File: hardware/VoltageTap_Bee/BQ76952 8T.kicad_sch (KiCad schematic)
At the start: 113 parts, among them U201 2PD2150-QX, U202 2PD2150-QX, U203 2PD2150-QX, U204 2PD2150-QX, U205 2PD2150-QX, U206 2PD2150-QX, U207 2PD2150-QX, U208 2PD2150-QX, U209 2PD2150-QX, U210 2PD2150-QX, U211 2PD2150-QX, U212 2PD2150-QX, U213 2PD2150-QX, U214 2PD2150-QX, U215 2PD2150-QX, U216 2PD2150-QX, U217 PBQ76952PFBT, U218 FCX495

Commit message: This is a cry for help
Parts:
- removed D218: ES1D, Diode_SMD:D_SMA, symbol Device:D_Schottky_Small
- removed R255: 100, Resistor_SMD:R_0805_2012Metric, symbol Device:R_Small_US
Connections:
- net 16P: now also U218.2
- net BAT: now also C221.1
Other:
- note removed: "joined to prevent absurd voltage differences"
- moved on the sheet: C220, C221

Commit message: uhhh
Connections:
- net 16P: no longer R253.2, R254.1, U218.2
- net at D217.1 (K), R252.2: now also R253.2, R254.1, U218.2
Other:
- added sheet something (../common designs.kicad_sch)
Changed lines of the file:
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@@
 	)
 	(junction
-		(at 246.38 16.51)
-		(diameter 0)
-		(color 0 0 0 0)
-	)
-	(junction
 		(at 127 114.3)
 		(diameter 0)
@@
 	)
 	(junction
+		(at 246.38 26.67)
+		(diameter 0)
+		(color 0 0 0 0)
+	)
+	(junction
 		(at 149.86 96.52)
 		(diameter 0)
@@
 	(wire
 		(pts
-			(xy 262.89 16.51) (xy 262.89 72.39)
-		)
-		(stroke
-			(width 0)
-			(type default)
-		)
-	)
-	(wire
-		(pts
 			(xy 148.59 35.56) (xy 149.86 36.83)
 		)
@@
 	(wire
 		(pts
+			(xy 262.89 26.67) (xy 262.89 72.39)
+		)
+		(stroke
+			(width 0)
+			(type default)
+		)
+	)
+	(wire
+		(pts
 			(xy 196.85 59.69) (xy 198.12 59.69)
 		)
@@
 	(wire
 		(pts
-			(xy 246.38 16.51) (xy 262.89 16.51)
-		)
-		(stroke
-			(width 0)
-			(type default)
-		)
-	)
-	(wire
-		(pts
 			(xy 55.88 31.75) (xy 64.77 31.75)
 		)
@@
 	(wire
 		(pts
+			(xy 246.38 26.67) (xy 246.38 33.02)
+		)
+		(stroke
+			(width 0)
+			(type default)
+		)
+	)
+	(wire
+		(pts
 			(xy 55.88 130.81) (xy 55.88 132.08)
 		)
@@
 	(wire
 		(pts
+			(xy 246.38 26.67) (xy 262.89 26.67)
+		)
+		(stroke
+			(width 0)
+			(type default)
+		)
+	)
+	(wire
+		(pts
 			(xy 226.06 48.26) (xy 237.49 48.26)
 		)
@@
 	(wire
 		(pts
-			(xy 246.38 24.13) (xy 246.38 33.02)
+			(xy 246.38 24.13) (xy 246.38 26.67)
 		)
 		(stroke
@@
 				)
 			)
+		)
+	)
+	(sheet
+		(at 347.98 172.72)
+		(size 27.94 22.86)
+		(exclude_from_sim yes)
+		(in_bom no)
+		(on_board no)
+		(dnp yes)
+		(fields_autoplaced yes)
+		(stroke
+			(width 0.1524)
+			(type solid)
+		)
+		(fill
+			(color 0 0 0 0.0000)
+		)
+		(property "Sheetname" "something"
+			(at 347.98 172.0084 0)
+			(effects
+				(font
+					(size 1.27 1.27)
+				)
+				(justify left bottom)
+			)
+		)
+		(property "Sheetfile" "../common designs.kicad_sch"
+			(at 347.98 196.1646 0)
+			(effects
+				(font
+					(size 1.27 1.27)
+				)
+				(justify left top)
+			)
+		)
+		(property "Field2" ""
+			(at 347.98 172.72 0)
+			(effects
+				(font
+					(size 1.27 1.27)
+				)
+			)
+		)
+		(instances
+			(project "VoltageTap_B"
+				(path "/24c6cb45-cbeb-4148-a23c-ec2e76234670/5ed1aefd-4d0e-4d3d-a5a2-f479b00e73a5"
+					(page "5")
+				)
+			)

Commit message: aenllaec
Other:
- removed sheet something
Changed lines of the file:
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@@
-		)
-	)
-	(sheet
-		(at 347.98 172.72)
-		(size 27.94 22.86)
-		(exclude_from_sim yes)
-		(in_bom no)
-		(on_board no)
-		(dnp yes)
-		(fields_autoplaced yes)
-		(stroke
-			(width 0.1524)
-			(type solid)
-		)
-		(fill
-			(color 0 0 0 0.0000)
-		)
-		(property "Sheetname" "something"
-			(at 347.98 172.0084 0)
-			(effects
-				(font
-					(size 1.27 1.27)
-				)
-				(justify left bottom)
-			)
-		)
-		(property "Sheetfile" "../common designs.kicad_sch"
-			(at 347.98 196.1646 0)
-			(effects
-				(font
-					(size 1.27 1.27)
-				)
-				(justify left top)
-			)
-		)
-		(property "Field2" ""
-			(at 347.98 172.72 0)
-			(effects
-				(font
-					(size 1.27 1.27)
-				)
-			)
-		)
-		(instances
-			(project "VoltageTap_B"
-				(path "/24c6cb45-cbeb-4148-a23c-ec2e76234670/5ed1aefd-4d0e-4d3d-a5a2-f479b00e73a5"
-					(page "999")
-				)
-			)
 		)
 	)

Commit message: baeckbjlnacnklac
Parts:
- renumbered R256 to R255
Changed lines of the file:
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@@
 		(on_board yes)
 		(dnp no)
-		(property "Reference" "R256"
+		(property "Reference" "R255"
 			(at 274.828 82.55 0)
 			(effects
@@
 			(project "VoltageTap_B"
 				(path "/24c6cb45-cbeb-4148-a23c-ec2e76234670/5ed1aefd-4d0e-4d3d-a5a2-f479b00e73a5"
-					(reference "R256")
+					(reference "R255")
 					(unit 1)
 				)

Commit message: Fixing
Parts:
- R221, R222, R223, R224, R225, R226, R227, R245, R246, R247, R248, R249, R250, R251: mouser https://www.mouser.com/ProductDetail/KOA-Speer/RK73H2BTTD22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 -> https://www.mouser.com/ProductDetail/KOA-Speer/RK73H2ATTD22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
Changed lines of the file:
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@@
 			)
 		)
-		(property "mouser" "https://www.mouser.com/ProductDetail/KOA-Speer/RK73H2BTTD2260F?qs=sGAEpiMZZMvdGkrng054t0wRT%252B902PGcT6B0yBPcmBs%3D"
+		(property "mouser" "https://www.mouser.com/ProductDetail/KOA-Speer/RK73H2ATTD2260F?qs=MzOn2VpwozEuMvy0cV9RWw%3D%3D"
 			(at 67.31 147.32 0)
 			(effects
@@
 			)
 		)
-		(property "mouser" "https://www.mouser.com/ProductDetail/KOA-Speer/RK73H2BTTD2260F?qs=sGAEpiMZZMvdGkrng054t0wRT%252B902PGcT6B0yBPcmBs%3D"
+		(property "mouser" "https://www.mouser.com/ProductDetail/KOA-Speer/RK73H2ATTD2260F?qs=MzOn2VpwozEuMvy0cV9RWw%3D%3D"
 			(at 138.43 46.99 0)
 			(effects
@@
 			)
 		)
-		(property "mouser" "https://www.mouser.com/ProductDetail/KOA-Speer/RK73H2BTTD2260F?qs=sGAEpiMZZMvdGkrng054t0wRT%252B902PGcT6B0yBPcmBs%3D"
+		(property "mouser" "https://www.mouser.com/ProductDetail/KOA-Speer/RK73H2ATTD2260F?qs=MzOn2VpwozEuMvy0cV9RWw%3D%3D"
 			(at 138.43 96.52 0)
 			(effects
@@
 			)
 		)
-		(property "mouser" "https://www.mouser.com/ProductDetail/KOA-Speer/RK73H2BTTD2260F?qs=sGAEpiMZZMvdGkrng054t0wRT%252B902PGcT6B0yBPcmBs%3D"
+		(property "mouser" "https://www.mouser.com/ProductDetail/KOA-Speer/RK73H2ATTD2260F?qs=MzOn2VpwozEuMvy0cV9RWw%3D%3D"
 			(at 67.31 97.79 0)
 			(effects
@@
 			)
 		)
-		(property "mouser" "https://www.mouser.com/ProductDetail/KOA-Speer/RK73H2BTTD2260F?qs=sGAEpiMZZMvdGkrng054t0wRT%252B902PGcT6B0yBPcmBs%3D"
+		(property "mouser" "https://www.mouser.com/ProductDetail/KOA-Speer/RK73H2ATTD2260F?qs=MzOn2VpwozEuMvy0cV9RWw%3D%3D"
 			(at 67.31 163.83 0)
 			(effects
@@
 			)
 		)
-		(property "mouser" "https://www.mouser.com/ProductDetail/KOA-Speer/RK73H2BTTD2260F?qs=sGAEpiMZZMvdGkrng054t0wRT%252B902PGcT6B0yBPcmBs%3D"
+		(property "mouser" "https://www.mouser.com/ProductDetail/KOA-Speer/RK73H2ATTD2260F?qs=MzOn2VpwozEuMvy0cV9RWw%3D%3D"
 			(at 138.43 114.3 0)
 			(effects
@@
 			)
 		)
-		(property "mouser" "https://www.mouser.com/ProductDetail/KOA-Speer/RK73H2BTTD2260F?qs=sGAEpiMZZMvdGkrng054t0wRT%252B902PGcT6B0yBPcmBs%3D"
+		(property "mouser" "https://www.mouser.com/ProductDetail/KOA-Speer/RK73H2ATTD2260F?qs=MzOn2VpwozEuMvy0cV9RWw%3D%3D"
 			(at 138.43 130.81 0)
 			(effects
@@
 			)
 		)
-		(property "mouser" "https://www.mouser.com/ProductDetail/KOA-Speer/RK73H2BTTD2260F?qs=sGAEpiMZZMvdGkrng054t0wRT%252B902PGcT6B0yBPcmBs%3D"
+		(property "mouser" "https://www.mouser.com/ProductDetail/KOA-Speer/RK73H2ATTD2260F?qs=MzOn2VpwozEuMvy0cV9RWw%3D%3D"
 			(at 138.43 63.5 0)
 			(effects
@@
 			)
 		)
-		(property "mouser" "https://www.mouser.com/ProductDetail/KOA-Speer/RK73H2BTTD2260F?qs=sGAEpiMZZMvdGkrng054t0wRT%252B902PGcT6B0yBPcmBs%3D"
+		(property "mouser" "https://www.mouser.com/ProductDetail/KOA-Speer/RK73H2ATTD2260F?qs=MzOn2VpwozEuMvy0cV9RWw%3D%3D"
 			(at 138.43 80.01 0)
 			(effects
@@
 			)
 		)
-		(property "mouser" "https://www.mouser.com/ProductDetail/KOA-Speer/RK73H2BTTD2260F?qs=sGAEpiMZZMvdGkrng054t0wRT%252B902PGcT6B0yBPcmBs%3D"
+		(property "mouser" "https://www.mouser.com/ProductDetail/KOA-Speer/RK73H2ATTD2260F?qs=MzOn2VpwozEuMvy0cV9RWw%3D%3D"
 			(at 67.31 130.81 0)
 			(effects
@@
 			)
 		)
-		(property "mouser" "https://www.mouser.com/ProductDetail/KOA-Speer/RK73H2BTTD2260F?qs=sGAEpiMZZMvdGkrng054t0wRT%252B902PGcT6B0yBPcmBs%3D"
+		(property "mouser" "https://www.mouser.com/ProductDetail/KOA-Speer/RK73H2ATTD2260F?qs=MzOn2VpwozEuMvy0cV9RWw%3D%3D"
 			(at 67.31 64.77 0)
 			(effects
@@
 			)
 		)
-		(property "mouser" "https://www.mouser.com/ProductDetail/KOA-Speer/RK73H2BTTD2260F?qs=sGAEpiMZZMvdGkrng054t0wRT%252B902PGcT6B0yBPcmBs%3D"
+		(property "mouser" "https://www.mouser.com/ProductDetail/KOA-Speer/RK73H2ATTD2260F?qs=MzOn2VpwozEuMvy0cV9RWw%3D%3D"
 			(at 67.31 114.3 0)
 			(effects
@@
 			)
 		)
-		(property "mouser" "https://www.mouser.com/ProductDetail/KOA-Speer/RK73H2BTTD2260F?qs=sGAEpiMZZMvdGkrng054t0wRT%252B902PGcT6B0yBPcmBs%3D"
+		(property "mouser" "https://www.mouser.com/ProductDetail/KOA-Speer/RK73H2ATTD2260F?qs=MzOn2VpwozEuMvy0cV9RWw%3D%3D"
 			(at 67.31 81.28 0)
 			(effects
@@
 			)
 		)
-		(property "mouser" "https://www.mouser.com/ProductDetail/KOA-Speer/RK73H2BTTD2260F?qs=sGAEpiMZZMvdGkrng054t0wRT%252B902PGcT6B0yBPcmBs%3D"
+		(property "mouser" "https://www.mouser.com/ProductDetail/KOA-Speer/RK73H2ATTD2260F?qs=MzOn2VpwozEuMvy0cV9RWw%3D%3D"
 			(at 138.43 147.32 0)
 			(effects

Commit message: added part numbers for mouser
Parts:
- C203, C204, C205, C206, C207, C208, C209, C211, C212, C213, C214, C215, C216, C217: Mouser Part Number (none) -> 710-885012206095
- C219: Mouser Part Number (none) -> 187-CL31A106KBHNNNE
- C220, C221: Mouser Part Number (none) -> 187-CL31B105KCHNNNE
- D203, D204, D205, D206, D207, D208, D209, D210, D211, D212, D213, D214, D215, D216: Mouser Part Number (none) -> 821-TS4148RBG
- D217: Mouser Part Number (none) -> 512-ES1C
- R203, R204, R205, R206, R207, R208, R209, R228, R229, R230, R231, R232, R233, R234: Mouser Part Number (none) -> 755-LTR100JZPJ360
- R212, R213, R214, R215, R216, R217, R218, R237, R238, R239, R240, R241, R242, R243, R244, R252: Mouser Part Number (none) -> 660-SG73S2ATTD101J
- R221, R222, R223, R224, R225, R226, R227, R245, R246, R247, R248, R249, R250, R251: Mouser Part Number (none) -> 660-RK73H2ATTD2260F
- R253, R255: Mouser Part Number (none) -> 603-AC0805FR-7W10KL
- R254: Mouser Part Number (none) -> 708-RNCP1206FTD4K99
- U203, U204, U205, U206, U207, U208, U209, U210, U211, U212, U213, U214, U215, U216: Mouser Part Number (none) -> 771-2PD2150-QX
- U217: Mouser Part Number (none) -> 595-BQ7697204PFBR
- U218: Mouser Part Number (none) -> 522-FCX495TA

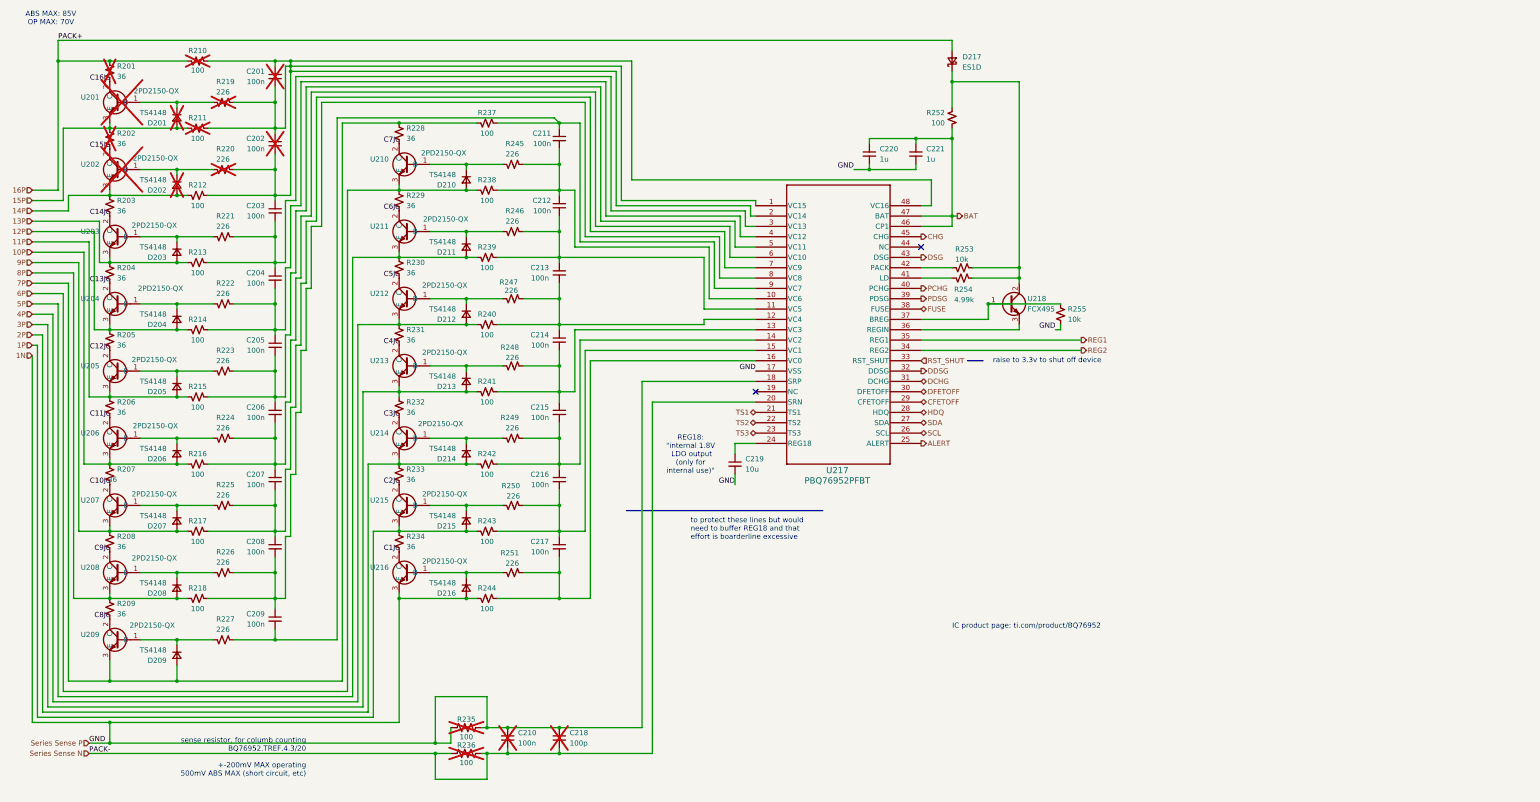
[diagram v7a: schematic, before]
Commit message: rework vt bee
UTA, where CpEs cant make a pcb and CSs cant write any code.
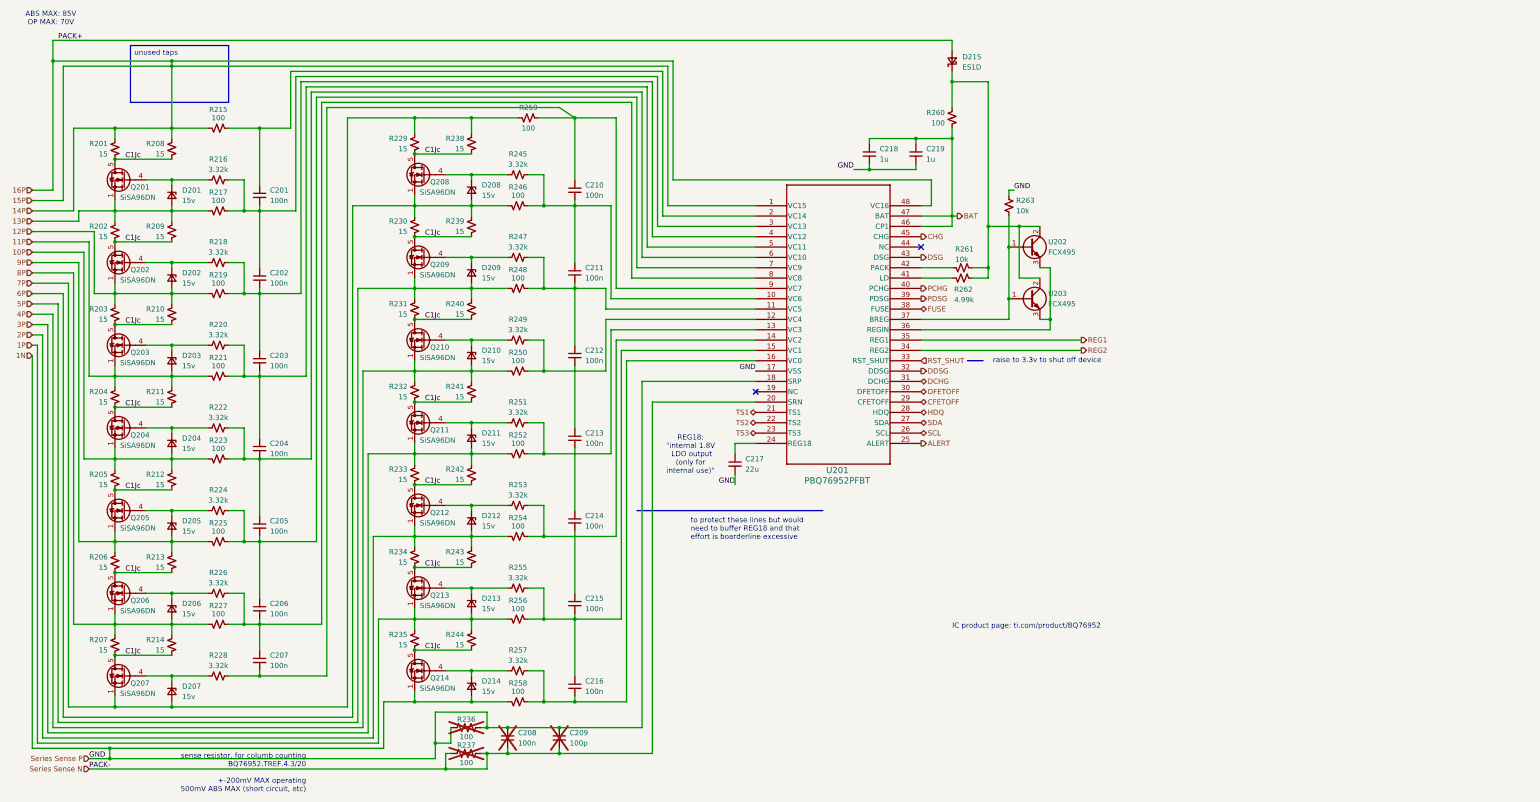
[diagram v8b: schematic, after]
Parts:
- removed C201, C202, C205, C216: 100n, Capacitor_SMD:C_0603_1608Metric_Pad1.08x0.95mm_HandSolder, symbol Device:C_Small
- removed C219: 10u, Capacitor_SMD:C_1206_3216Metric_Pad1.33x1.80mm_HandSolder, symbol Device:C_Small
- removed D201, D202, D203, D204, D205, D206, D207, D208, D209, D210, D211, D212, D213, D214, D215, D216: TS4148, Diode_SMD:D_0805_2012Metric_Pad1.15x1.40mm_HandSolder, symbol Device:D_Small
- removed U201, U202, U203, U204, U205, U206, U207, U208, U209, U210, U211, U212, U213, U214, U215, U216: 2PD2150-QX, Package_TO_SOT_SMD:SOT-89-3, symbol zzLocalLibrary:2PD2150-QX
- added C207, C210: 100n, Capacitor_SMD:C_0603_1608Metric_Pad1.08x0.95mm_HandSolder, symbol Device:C_Small
- added C217: 22u, Capacitor_SMD:C_0805_2012Metric_Pad1.18x1.45mm_HandSolder, symbol Device:C_Small
- added D201, D202, D203, D204, D205, D206, D207, D208, D209, D210, D211, D212, D213, D214: 15v, Diode_SMD:D_SOD-123, symbol Device:D_Zener_Small
- added Q201, Q202, Q203, Q204, Q205, Q206, Q207, Q208, Q209, Q210, Q211, Q212, Q213, Q214: SiSA96DN, Package_SO:Vishay_PowerPAK_1212-8_Single, symbol Transistor_FET:SiS454DN
- added R234, R244: 15, zzLocalLibraries-Footprints:imperial wide resistor R_ 3264, symbol Device:R_Small_US
- added R252, R254, R256: 100, Resistor_SMD:R_0805_2012Metric, symbol Device:R_Small_US
- added R253, R255, R257: 3.32k, Resistor_SMD:R_0805_2012Metric_Pad1.20x1.40mm_HandSolder, symbol Device:R_Small_US
- added U203: FCX495, Package_TO_SOT_SMD:SOT-89-3, symbol zzLocalLibrary:FCX485_NPN_BJT
- R201, R202: value 36 -> 15; Mouser Part Number (none) -> 755-LTR100JZPJ360; mouser https://www.mouser.com/ProductDetail/ROHM-Semiconductor/LTR100JZPJ360?qs=sGAEpiMZZMvdGkrng054tx4c7YuULGmGPstrAxlE1rsJ3%252BFyNXvM0g%3D%3D -> https://www.mouser.com/ProductDetail/ROHM-Semiconductor/LTR100JZPJ150?qs=Y0Uzf4wQF3lnWrANyJBr0A%3D%3D; specs 36 ohm, 3W, 200V, 1%, surge, wide. 200ppm, -55C, +155C -> 15 ohm, 3W, 200V, 1%, surge, wide. 200ppm, -55C, +155C; now fitted; now in the parts list
- R203, R204, R205, R206, R207, R208, R209, R229, R230, R231, R232, R233: value 36 -> 15; mouser https://www.mouser.com/ProductDetail/ROHM-Semiconductor/LTR100JZPJ360?qs=sGAEpiMZZMvdGkrng054tx4c7YuULGmGPstrAxlE1rsJ3%252BFyNXvM0g%3D%3D -> https://www.mouser.com/ProductDetail/ROHM-Semiconductor/LTR100JZPJ150?qs=Y0Uzf4wQF3lnWrANyJBr0A%3D%3D; specs 36 ohm, 3W, 200V, 1%, surge, wide. 200ppm, -55C, +155C -> 15 ohm, 3W, 200V, 1%, surge, wide. 200ppm, -55C, +155C
- R210, R211: value 100 -> 15; footprint Resistor_SMD:R_0805_2012Metric -> zzLocalLibraries-Footprints:imperial wide resistor R_ 3264; Mouser Part Number (none) -> 755-LTR100JZPJ360; mouser https://www.mouser.com/ProductDetail/KOA-Speer/SG73S2ATTD10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 -> https://www.mouser.com/ProductDetail/ROHM-Semiconductor/LTR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; specs 100 omh, thick, anti surge, 5%, 750mW, 400V, -55C, +155C, 1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 -> 15 ohm, 3W, 200V, 1%, surge, wide. 200ppm, -55C, +155C; unit x1 0.12 -> 0.60; unit x10 0.037 -> 0.265; unit x100 (none) -> 0.214; now fitted; now in the parts list
- R212, R213, R214, R238, R239, R240, R241, R242, R243: value 100 -> 15; footprint Resistor_SMD:R_0805_2012Metric -> zzLocalLibraries-Footprints:imperial wide resistor R_ 3264; Mouser Part Number 660-SG73S2ATTD101J -> 755-LTR100JZPJ360; mouser https://www.mouser.com/ProductDetail/KOA-Speer/SG73S2ATTD10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 -> https://www.mouser.com/ProductDetail/ROHM-Semiconductor/LTR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; specs 100 omh, thick, anti surge, 5%, 750mW, 400V, -55C, +155C, 1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 -> 15 ohm, 3W, 200V, 1%, surge, wide. 200ppm, -55C, +155C; unit x1 0.12 -> 0.60; unit x10 0.037 -> 0.265; unit x100 (none) -> 0.214
- R216, R218: value 100 -> 3.32k; footprint Resistor_SMD:R_0805_2012Metric -> Resistor_SMD:R_0805_2012Metric_Pad1.20x1.40mm_HandSolder; Mouser Part Number 660-SG73S2ATTD101J -> (none); mouser https://www.mouser.com/ProductDetail/KOA-Speer/SG73S2ATTD10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 -> https://www.mouser.com/ProductDetail/Walsin/WR08X3321FTL?qs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; specs 100 omh, thick, anti surge, 5%, 750mW, 400V, -55C, +155C, 1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 -> 3.32kOhm, 1%, 150V, 125mW, 100ppm, -55C, 155C; unit x1 0.12 -> 0.10; unit x10 0.037 -> .025
- R219: value 226 -> 100; footprint Resistor_SMD:R_0805_2012Metric_Pad1.20x1.40mm_HandSolder -> Resistor_SMD:R_0805_2012Metric; Mouser Part Number (none) -> 660-SG73S2ATTD101J; mouser https://www.mouser.com/ProductDetail/KOA-Speer/RK73H2BTTD22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 -> https://www.mouser.com/ProductDetail/KOA-Speer/SG73S2ATTD10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; specs 226Ohm, 250mW, 1%, 200V, -55C, +155C -> 100 omh, thick, anti surge, 5%, 750mW, 400V, -55C, +155C, 1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; unit x1 0.10 -> 0.12; unit x10 0.023 -> 0.037; now fitted; now in the parts list
- R220: value 226 -> 3.32k; mouser https://www.mouser.com/ProductDetail/KOA-Speer/RK73H2BTTD22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 -> https://www.mouser.com/ProductDetail/Walsin/WR08X3321FTL?qs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; specs 226Ohm, 250mW, 1%, 200V, -55C, +155C -> 3.32kOhm, 1%, 150V, 125mW, 100ppm, -55C, 155C; unit x10 0.023 -> .025; now fitted; now in the parts list
- R221, R223, R225, R227, R246, R248, R250: value 226 -> 100; footprint Resistor_SMD:R_0805_2012Metric_Pad1.20x1.40mm_HandSolder -> Resistor_SMD:R_0805_2012Metric; Mouser Part Number 660-RK73H2ATTD2260F -> 660-SG73S2ATTD101J; mouser https://www.mouser.com/ProductDetail/KOA-Speer/RK73H2ATTD22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 -> https://www.mouser.com/ProductDetail/KOA-Speer/SG73S2ATTD10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; specs 226Ohm, 250mW, 1%, 200V, -55C, +155C -> 100 omh, thick, anti surge, 5%, 750mW, 400V, -55C, +155C, 1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; unit x1 0.10 -> 0.12; unit x10 0.023 -> 0.037
- R222, R224, R226, R245, R247, R249, R251: value 226 -> 3.32k; Mouser Part Number 660-RK73H2ATTD2260F -> (none); mouser https://www.mouser.com/ProductDetail/KOA-Speer/RK73H2ATTD22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 -> https://www.mouser.com/ProductDetail/Walsin/WR08X3321FTL?qs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; specs 226Ohm, 250mW, 1%, 200V, -55C, +155C -> 3.32kOhm, 1%, 150V, 125mW, 100ppm, -55C, 155C; unit x10 0.023 -> .025
- R228: value 36 -> 3.32k; footprint zzLocalLibraries-Footprints:imperial wide resistor R_ 3264 -> Resistor_SMD:R_0805_2012Metric_Pad1.20x1.40mm_HandSolder; Mouser Part Number 755-LTR100JZPJ360 -> (none); mouser https://www.mouser.com/ProductDetail/ROHM-Semiconductor/LTR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 -> https://www.mouser.com/ProductDetail/Walsin/WR08X3321FTL?qs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; specs 36 ohm, 3W, 200V, 1%, surge, wide. 200ppm, -55C, +155C -> 3.32kOhm, 1%, 150V, 125mW, 100ppm, -55C, 155C; unit x1 0.60 -> 0.10; unit x10 0.265 -> .025; unit x100 0.214 -> (none)
- R235: renamed from R234; value 36 -> 15; mouser https://www.mouser.com/ProductDetail/ROHM-Semiconductor/LTR100JZPJ360?qs=sGAEpiMZZMvdGkrng054tx4c7YuULGmGPstrAxlE1rsJ3%252BFyNXvM0g%3D%3D -> https://www.mouser.com/ProductDetail/ROHM-Semiconductor/LTR100JZPJ150?qs=Y0Uzf4wQF3lnWrANyJBr0A%3D%3D; specs 36 ohm, 3W, 200V, 1%, surge, wide. 200ppm, -55C, +155C -> 15 ohm, 3W, 200V, 1%, surge, wide. 200ppm, -55C, +155C
- renumbered C203 to C201, C204 to C202, C206 to C203, C207 to C204, C208 to C205, C209 to C206, C210 to C208, C218 to C209, C217 to C216, C220 to C218, C221 to C219, D217 to D215, R235 to R236, R236 to R237, R244 to R258, R237 to R259, R252 to R260, R253 to R261, R254 to R262, R255 to R263, U217 to U201, U218 to U202
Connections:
- net C10Jc is gone; now on net C1Jc: R207.1
- net C11Jc is gone; now on net C1Jc: R206.1
- net C12Jc is gone; now on net C1Jc: R205.1
- net C13Jc is gone; now on net C1Jc: R204.1
- net C14Jc is gone; now on net C1Jc: R203.1
- net C15Jc is gone; now on net C1Jc: R202.1
- net C16Jc is gone; now on net C1Jc: R201.1
- net C2Jc is gone; now on net C1Jc: R233.1
- net C3Jc is gone; now on net C1Jc: R232.1
- net C4Jc is gone; now on net C1Jc: R231.1
- net C5Jc is gone; now on net C1Jc: R230.1
- net C6Jc is gone; now on net C1Jc: R229.1
- net C8Jc is gone; now on net C1Jc: R209.1
- net C9Jc is gone; now on net C1Jc: R208.1
- net 10P: now also R205.2, R212.2, R223.2, D204.2 (A), Q204.1 (S), Q204.2 (S), Q204.3 (S); no longer R207.2, R216.2
- net 11P: now also R204.2, R211.2, R221.2, D203.2 (A), Q203.1 (S), Q203.2 (S), Q203.3 (S); no longer R206.2, R215.2
- net 12P: now also R203.2, R210.2, R219.2, D202.2 (A), Q202.1 (S), Q202.2 (S), Q202.3 (S); no longer R205.2, R214.2
- net 13P: now also R202.2, R209.2, R217.2, D201.2 (A), Q201.1 (S), Q201.2 (S), Q201.3 (S); no longer R204.2, R213.2
- net 14P: now also D215.2 (A), R201.2, R208.2, R215.2, U201.1 (VC15), U201.48 (VC16); no longer R203.2, R212.2
- net 1N: now also R263.2, C217.2, D214.2 (A), Q214.1 (S), Q214.2 (S), Q214.3 (S); no longer R263.1
- net 1P: now also D213.2 (A), Q213.1 (S), Q213.2 (S), Q213.3 (S), R244.2, R256.2; no longer R243.2
- net 2P: now also R243.2, D212.2 (A), Q212.1 (S), Q212.2 (S), Q212.3 (S), R234.2, R254.2; no longer R233.2, R242.2
- net 3P: now also R233.2, R242.2, D211.2 (A), Q211.1 (S), Q211.2 (S), Q211.3 (S), R252.2; no longer R232.2, R241.2
- net 4P: now also R232.2, R241.2, R250.2, D210.2 (A), Q210.1 (S), Q210.2 (S), Q210.3 (S); no longer R231.2, R240.2
- net 5P: now also R231.2, R240.2, R248.2, D209.2 (A), Q209.1 (S), Q209.2 (S), Q209.3 (S); no longer R230.2, R239.2
- net 6P: now also R230.2, R239.2, R246.2, D208.2 (A), Q208.1 (S), Q208.2 (S), Q208.3 (S); no longer R229.2, R238.2
- net 7P: now also R229.2, R238.2, D207.2 (A), Q207.1 (S), Q207.2 (S), Q207.3 (S); no longer R228.2
- net 8P: now also R207.2, R214.2, R227.2, D206.2 (A), Q206.1 (S), Q206.2 (S), Q206.3 (S); no longer R209.2, R218.2
- net 9P: now also R206.2, R213.2, R225.2, D205.2 (A), Q205.1 (S), Q205.2 (S), Q205.3 (S); no longer R208.2, R217.2
- net C1Jc: now also R210.1, R211.1, R212.1, R213.1, R214.1, R238.1, R239.1, R240.1, R241.1, R242.1, R243.1, Q201.5 (D), Q202.5 (D), Q203.5 (D), Q204.5 (D), Q205.5 (D), Q206.5 (D), Q207.5 (D), Q208.5 (D), Q209.5 (D), Q210.5 (D), Q211.5 (D), Q212.5 (D), Q213.5 (D), Q214.5 (D), R234.1, R244.1
- net at R226.2: now also C206.2, R227.1, U201.8 (VC8), C207.1
- net at C201.2, C202.1, U201.3 (VC13): now also R216.2, R217.1; no longer R213.1, R221.1
- net at C216.2, R258.1, U201.16 (VC0): now also R257.2; no longer R251.1
- net at R247.2: now also C211.2, C212.1, R248.1, U201.11 (VC5)
- net at U201.37 (BREG), U202.1: now also R263.1, U203.1; no longer R263.2
- net at R245.2: now also C211.1, R246.1, U201.10 (VC6), C210.2
- net at C202.2, U201.4 (VC12): now also C203.1, R218.2, R219.1; no longer R214.1, R222.1
- net at D215.1 (K), R260.2, R261.2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: now also U203.2
- net at U201.36 (REGIN), U202.3: now also U203.3
- net at C216.1, U201.15 (VC1): now also C215.2, R255.2, R256.1; no longer R243.1, R250.1
- net at R222.2: now also C204.2, C205.1, R223.1, U201.6 (VC10)
- net at R251.2: now also U201.13 (VC3), R252.1
- net at R249.2: now also R250.1, U201.12 (VC4)
- net at U201.24 (REG18): now also C217.1
- net at R220.2: now also C203.2, C204.1, R221.1, U201.5 (VC11)
- net at R224.2: now also C205.2, C206.1, R225.1, U201.7 (VC9)
- removed net 15P: R202.2, R211.2
- removed net 16P: D215.2 (A), R201.2, R210.2
- net C7Jc: no longer names the net of R228.1
- net C7Jc: now also D207.1 (K), Q207.4 (G)
- new net: D202.1 (K), Q202.4 (G), R218.1
- new net: D213.1 (K), Q213.4 (G), R255.1
- new net: C201.1, R215.1, U201.2 (VC14)
- new net: D203.1 (K), Q203.4 (G), R220.1
- new net: D205.1 (K), Q205.4 (G), R224.1
- new net: D204.1 (K), Q204.4 (G), R222.1
- new net: D212.1 (K), Q212.4 (G), R253.1
- new net: R253.2, R254.1, U201.14 (VC2)
- new net: D208.1 (K), Q208.4 (G), R245.1
- new net: D201.1 (K), Q201.4 (G), R216.1
- new net: D214.1 (K), Q214.4 (G), R257.1
- new net: D209.1 (K), Q209.4 (G), R247.1
- new net: D210.1 (K), Q210.4 (G), R249.1
- new net: D211.1 (K), Q211.4 (G), R251.1
- new net: D206.1 (K), Q206.4 (G), R226.1
- new net: C207.2, C210.1, R228.2, R259.1, U201.9 (VC7)
- new net: C214.2, C215.1
- new net: C213.2, C214.1
- new net: C212.2, C213.1
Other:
- moved on the sheet: C201, C202, C203, C204, C205, C206, C216, R235, R258, R259, R263, U202
